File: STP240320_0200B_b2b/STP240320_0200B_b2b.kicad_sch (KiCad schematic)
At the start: 2 parts, among them J1 Conn_02x08_Odd_Even

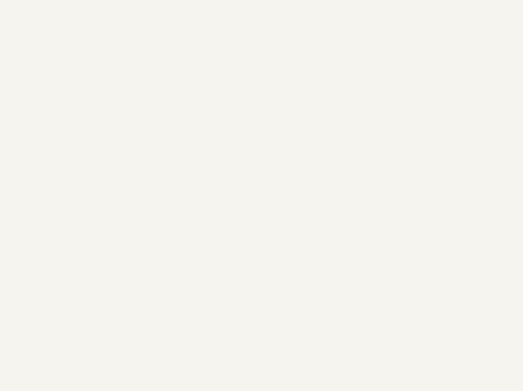
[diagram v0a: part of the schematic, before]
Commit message: all: cleanup revision info
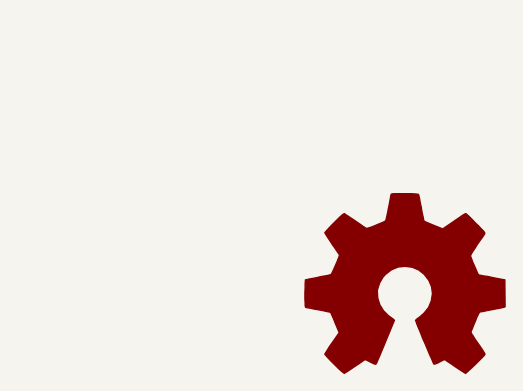
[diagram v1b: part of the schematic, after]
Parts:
- added SYM1: Logo_Open_Hardware_Large, Gigahawk:OSHW-Logo2_1.3x1.3mm_Mask, symbol Graphic:Logo_Open_Hardware_Large
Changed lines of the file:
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@@
     (title "STP240320_0200B Board to Board Connector Adapter")
     (date "${DATE}")
-    (rev "${TAG} (${REVISION})")
+    (rev "${TAG} (${HASH})")
   )
   (junction (at 96.52 60.96) (diameter 0) (color 0 0 0 0)
@@
         )
       )
+    )
+  )
+  (symbol (lib_id "Graphic:Logo_Open_Hardware_Large") (at 266.7 151.13 0) (unit 1)
+    (in_bom no) (on_board yes) (dnp no) (fields_autoplaced)
+    (property "Reference" "SYM1" (at 266.7 138.43 0)
+      (effects (font (size 1.27 1.27)) hide)
+    )
+    (property "Value" "Logo_Open_Hardware_Large" (at 266.7 161.29 0)
+      (effects (font (size 1.27 1.27)) hide)
+    )
+    (property "Footprint" "Gigahawk:OSHW-Logo2_1.3x1.3mm_Mask" (at 266.7 151.13 0)
+      (effects (font (size 1.27 1.27)) hide)
+    )
+    (property "Datasheet" "~" (at 266.7 151.13 0)
+      (effects (font (size 1.27 1.27)) hide)
+    )
+    (property "Sim.Enable" "0" (at 266.7 151.13 0)
+      (effects (font (size 1.27 1.27)) hide)
+    )
+    (instances
+      (project "STP240320_0200B_b2b"
+        (path "/194cbf42-24cc-40a5-a66b-fffb1517d1f4"
+          (reference "SYM1") (unit 1)
+        )
+      )
